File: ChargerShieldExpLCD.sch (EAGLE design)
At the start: 107 parts, among them IC1 TL431, IC2 LM324N, Q1 BUZ11, Q2 BD648, Q3 BUZ171, Q4 IRFZ48Z, T1 BC548, X1 +Vin, X2 VCC, X3 Battery

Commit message: rearranged power transistors
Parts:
- D1: device diode:SCHOTTKY-DIODEDO35-7 -> diode:SCHOTTKY-DIODEF126Z12
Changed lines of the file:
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@@
 <grid distance="0.05" unitdist="inch" unit="mm" style="lines" multiple="1" display="yes" altdistance="0.025" altunitdist="inch" altunit="mm"/>
 <layers>
-<layer number="1" name="Top" color="4" fill="1" visible="no" active="no"/>
-<layer number="2" name="Route2" color="1" fill="3" visible="no" active="no"/>
-<layer number="3" name="Route3" color="4" fill="3" visible="no" active="no"/>
-<layer number="4" name="Route4" color="1" fill="4" visible="no" active="no"/>
-<layer number="5" name="Route5" color="4" fill="4" visible="no" active="no"/>
-<layer number="6" name="Route6" color="1" fill="8" visible="no" active="no"/>
-<layer number="7" name="Route7" color="4" fill="8" visible="no" active="no"/>
-<layer number="8" name="Route8" color="1" fill="2" visible="no" active="no"/>
-<layer number="9" name="Route9" color="4" fill="2" visible="no" active="no"/>
-<layer number="10" name="Route10" color="1" fill="7" visible="no" active="no"/>
-<layer number="11" name="Route11" color="4" fill="7" visible="no" active="no"/>
-<layer number="12" name="Route12" color="1" fill="5" visible="no" active="no"/>
-<layer number="13" name="Route13" color="4" fill="5" visible="no" active="no"/>
-<layer number="14" name="Route14" color="1" fill="6" visible="no" active="no"/>
-<layer number="15" name="Route15" color="4" fill="6" visible="no" active="no"/>
-<layer number="16" name="Bottom" color="1" fill="1" visible="no" active="no"/>
-<layer number="17" name="Pads" color="2" fill="1" visible="no" active="no"/>
-<layer number="18" name="Vias" color="2" fill="1" visible="no" active="no"/>
-<layer number="19" name="Unrouted" color="6" fill="1" visible="no" active="no"/>
-<layer number="20" name="Dimension" color="15" fill="1" visible="no" active="no"/>
-<layer number="21" name="tPlace" color="7" fill="1" visible="no" active="no"/>
-<layer number="22" name="bPlace" color="7" fill="1" visible="no" active="no"/>
-<layer number="23" name="tOrigins" color="15" fill="1" visible="no" active="no"/>
-<layer number="24" name="bOrigins" color="15" fill="1" visible="no" active="no"/>
-<layer number="25" name="tNames" color="7" fill="1" visible="no" active="no"/>
-<layer number="26" name="bNames" color="7" fill="1" visible="no" active="no"/>
-<layer number="27" name="tValues" color="7" fill="1" visible="no" active="no"/>
-<layer number="28" name="bValues" color="7" fill="1" visible="no" active="no"/>
+<layer number="1" name="Top" color="4" fill="1" visible="yes" active="no"/>
+<layer number="2" name="Route2" color="1" fill="3" visible="yes" active="no"/>
+<layer number="3" name="Route3" color="4" fill="3" visible="yes" active="no"/>
+<layer number="4" name="Route4" color="1" fill="4" visible="yes" active="no"/>
+<layer number="5" name="Route5" color="4" fill="4" visible="yes" active="no"/>
+<layer number="6" name="Route6" color="1" fill="8" visible="yes" active="no"/>
+<layer number="7" name="Route7" color="4" fill="8" visible="yes" active="no"/>
+<layer number="8" name="Route8" color="1" fill="2" visible="yes" active="no"/>
+<layer number="9" name="Route9" color="4" fill="2" visible="yes" active="no"/>
+<layer number="10" name="Route10" color="1" fill="7" visible="yes" active="no"/>
+<layer number="11" name="Route11" color="4" fill="7" visible="yes" active="no"/>
+<layer number="12" name="Route12" color="1" fill="5" visible="yes" active="no"/>
+<layer number="13" name="Route13" color="4" fill="5" visible="yes" active="no"/>
+<layer number="14" name="Route14" color="1" fill="6" visible="yes" active="no"/>
+<layer number="15" name="Route15" color="4" fill="6" visible="yes" active="no"/>
+<layer number="16" name="Bottom" color="1" fill="1" visible="yes" active="no"/>
+<layer number="17" name="Pads" color="2" fill="1" visible="yes" active="no"/>
+<layer number="18" name="Vias" color="2" fill="1" visible="yes" active="no"/>
+<layer number="19" name="Unrouted" color="6" fill="1" visible="yes" active="no"/>
+<layer number="20" name="Dimension" color="15" fill="1" visible="yes" active="no"/>
+<layer number="21" name="tPlace" color="7" fill="1" visible="yes" active="no"/>
+<layer number="22" name="bPlace" color="7" fill="1" visible="yes" active="no"/>
+<layer number="23" name="tOrigins" color="15" fill="1" visible="yes" active="no"/>
+<layer number="24" name="bOrigins" color="15" fill="1" visible="yes" active="no"/>
+<layer number="25" name="tNames" color="7" fill="1" visible="yes" active="no"/>
+<layer number="26" name="bNames" color="7" fill="1" visible="yes" active="no"/>
+<layer number="27" name="tValues" color="7" fill="1" visible="yes" active="no"/>
+<layer number="28" name="bValues" color="7" fill="1" visible="yes" active="no"/>
 <layer number="29" name="tStop" color="7" fill="3" visible="no" active="no"/>
 <layer number="30" name="bStop" color="7" fill="6" visible="no" active="no"/>
@@
 <layer number="35" name="tGlue" color="7" fill="4" visible="no" active="no"/>
 <layer number="36" name="bGlue" color="7" fill="5" visible="no" active="no"/>
-<layer number="37" name="tTest" color="7" fill="1" visible="no" active="no"/>
-<layer number="38" name="bTest" color="7" fill="1" visible="no" active="no"/>
+<layer number="37" name="tTest" color="7" fill="1" visible="yes" active="no"/>
+<layer number="38" name="bTest" color="7" fill="1" visible="yes" active="no"/>
 <layer number="39" name="tKeepout" color="4" fill="11" visible="no" active="no"/>
 <layer number="40" name="bKeepout" color="1" fill="11" visible="no" active="no"/>
@@
 <layer number="44" name="Drills" color="7" fill="1" visible="no" active="no"/>
 <layer number="45" name="Holes" color="7" fill="1" visible="no" active="no"/>
-<layer number="46" name="Milling" color="3" fill="1" visible="no" active="no"/>
-<layer number="47" name="Measures" color="7" fill="1" visible="no" active="no"/>
-<layer number="48" name="Document" color="7" fill="1" visible="no" active="no"/>
-<layer number="49" name="Reference" color="7" fill="1" visible="no" active="no"/>
-<layer number="50" name="dxf" color="7" fill="1" visible="no" active="no"/>
-<layer number="51" name="tDocu" color="7" fill="1" visible="no" active="no"/>
-<layer number="52" name="bDocu" color="7" fill="1" visible="no" active="no"/>
-<layer number="53" name="tGND_GNDA" color="7" fill="9" visible="no" active="no"/>
-<layer number="54" name="bGND_GNDA" color="1" fill="9" visible="no" active="no"/>
-<layer number="56" name="wert" color="7" fill="1" visible="no" active="no"/>
-<layer number="57" name="tCAD" color="7" fill="1" visible="no" active="no"/>
+<layer number="46" name="Milling" color="3" fill="1" visible="yes" active="no"/>
+<layer number="47" name="Measures" color="7" fill="1" visible="yes" active="no"/>
+<layer number="48" name="Document" color="7" fill="1" visible="yes" active="no"/>
+<layer number="49" name="Reference" color="7" fill="1" visible="yes" active="no"/>
+<layer number="50" name="dxf" color="7" fill="1" visible="yes" active="no"/>
+<layer number="51" name="tDocu" color="7" fill="1" visible="yes" active="no"/>
+<layer number="52" name="bDocu" color="7" fill="1" visible="yes" active="no"/>
+<layer number="53" name="tGND_GNDA" color="7" fill="9" visible="yes" active="no"/>
+<layer number="54" name="bGND_GNDA" color="1" fill="9" visible="yes" active="no"/>
+<layer number="56" name="wert" color="7" fill="1" visible="yes" active="no"/>
+<layer number="57" name="tCAD" color="7" fill="1" visible="yes" active="no"/>
 <layer number="91" name="Nets" color="2" fill="1" visible="yes" active="yes"/>
 <layer number="92" name="Busses" color="1" fill="1" visible="yes" active="yes"/>
@@
 <part name="R16" library="rcl" deviceset="R-EU_" device="0207/10" value="1k"/>
 <part name="Q2" library="transistor-pnp" deviceset="BD648" device=""/>
-<part name="D1" library="diode" deviceset="SCHOTTKY-DIODE" device="DO35-7"/>
+<part name="D1" library="diode" deviceset="SCHOTTKY-DIODE" device="F126Z12"/>
 <part name="L1" library="rcl" deviceset="L-EU" device="0207/12" value="100µ"/>
 <part name="V1" library="Misc" deviceset="CELL" device=""/>

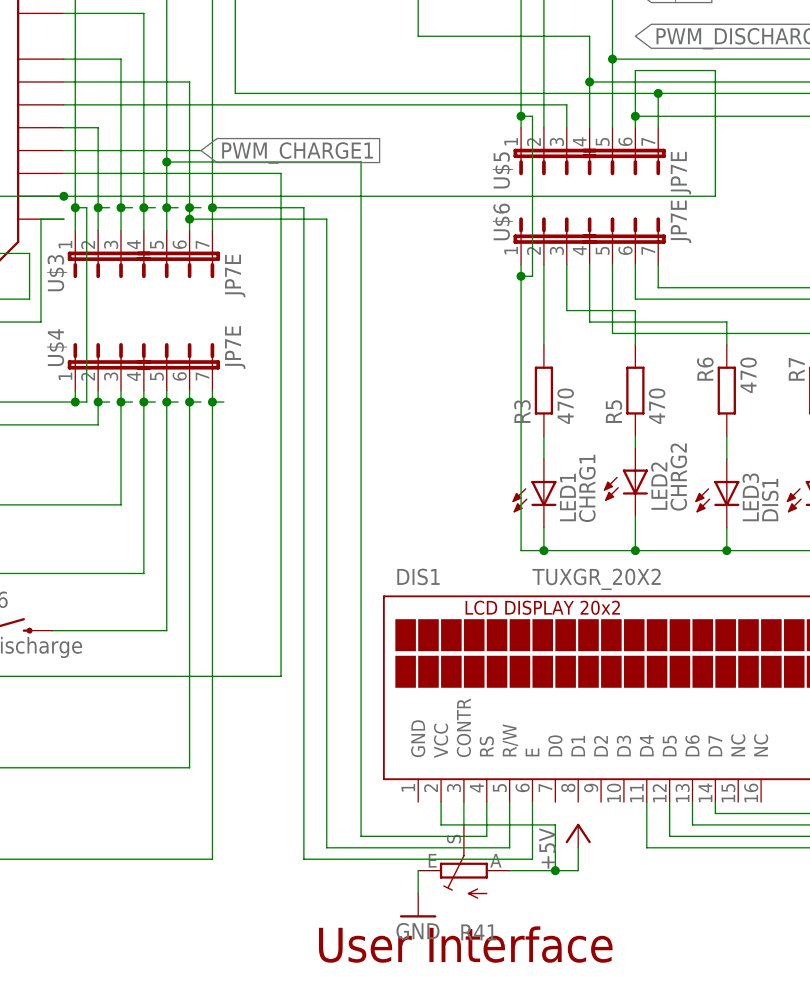
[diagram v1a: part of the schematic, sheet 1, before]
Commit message: jumper to switch LCD RS Pin
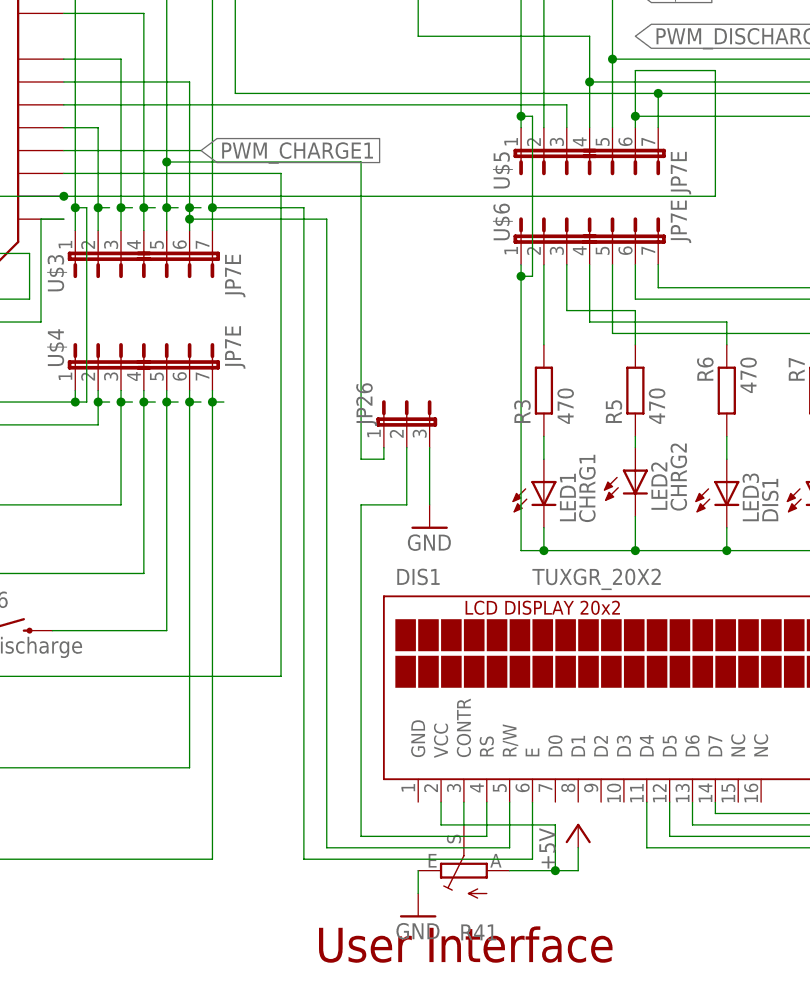
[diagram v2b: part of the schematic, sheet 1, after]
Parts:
- added JP26: (no value), bigger:JP2E
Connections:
- new net N$63: DIS1.RS, JP26.2
- net GND: now also JP26.3
- net N$67: now also JP26.1; no longer DIS1.RS
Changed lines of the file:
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@@
 <grid distance="0.05" unitdist="inch" unit="mm" style="lines" multiple="1" display="yes" altdistance="0.025" altunitdist="inch" altunit="mm"/>
 <layers>
-<layer number="1" name="Top" color="4" fill="1" visible="yes" active="no"/>
-<layer number="2" name="Route2" color="1" fill="3" visible="yes" active="no"/>
-<layer number="3" name="Route3" color="4" fill="3" visible="yes" active="no"/>
-<layer number="4" name="Route4" color="1" fill="4" visible="yes" active="no"/>
-<layer number="5" name="Route5" color="4" fill="4" visible="yes" active="no"/>
-<layer number="6" name="Route6" color="1" fill="8" visible="yes" active="no"/>
-<layer number="7" name="Route7" color="4" fill="8" visible="yes" active="no"/>
-<layer number="8" name="Route8" color="1" fill="2" visible="yes" active="no"/>
-<layer number="9" name="Route9" color="4" fill="2" visible="yes" active="no"/>
-<layer number="10" name="Route10" color="1" fill="7" visible="yes" active="no"/>
-<layer number="11" name="Route11" color="4" fill="7" visible="yes" active="no"/>
-<layer number="12" name="Route12" color="1" fill="5" visible="yes" active="no"/>
-<layer number="13" name="Route13" color="4" fill="5" visible="yes" active="no"/>
-<layer number="14" name="Route14" color="1" fill="6" visible="yes" active="no"/>
-<layer number="15" name="Route15" color="4" fill="6" visible="yes" active="no"/>
-<layer number="16" name="Bottom" color="1" fill="1" visible="yes" active="no"/>
-<layer number="17" name="Pads" color="2" fill="1" visible="yes" active="no"/>
-<layer number="18" name="Vias" color="2" fill="1" visible="yes" active="no"/>
-<layer number="19" name="Unrouted" color="6" fill="1" visible="yes" active="no"/>
-<layer number="20" name="Dimension" color="15" fill="1" visible="yes" active="no"/>
-<layer number="21" name="tPlace" color="7" fill="1" visible="yes" active="no"/>
-<layer number="22" name="bPlace" color="7" fill="1" visible="yes" active="no"/>
-<layer number="23" name="tOrigins" color="15" fill="1" visible="yes" active="no"/>
-<layer number="24" name="bOrigins" color="15" fill="1" visible="yes" active="no"/>
-<layer number="25" name="tNames" color="7" fill="1" visible="yes" active="no"/>
-<layer number="26" name="bNames" color="7" fill="1" visible="yes" active="no"/>
-<layer number="27" name="tValues" color="7" fill="1" visible="yes" active="no"/>
-<layer number="28" name="bValues" color="7" fill="1" visible="yes" active="no"/>
+<layer number="1" name="Top" color="4" fill="1" visible="no" active="no"/>
+<layer number="2" name="Route2" color="1" fill="3" visible="no" active="no"/>
+<layer number="3" name="Route3" color="4" fill="3" visible="no" active="no"/>
+<layer number="4" name="Route4" color="1" fill="4" visible="no" active="no"/>
+<layer number="5" name="Route5" color="4" fill="4" visible="no" active="no"/>
+<layer number="6" name="Route6" color="1" fill="8" visible="no" active="no"/>
+<layer number="7" name="Route7" color="4" fill="8" visible="no" active="no"/>
+<layer number="8" name="Route8" color="1" fill="2" visible="no" active="no"/>
+<layer number="9" name="Route9" color="4" fill="2" visible="no" active="no"/>
+<layer number="10" name="Route10" color="1" fill="7" visible="no" active="no"/>
+<layer number="11" name="Route11" color="4" fill="7" visible="no" active="no"/>
+<layer number="12" name="Route12" color="1" fill="5" visible="no" active="no"/>
+<layer number="13" name="Route13" color="4" fill="5" visible="no" active="no"/>
+<layer number="14" name="Route14" color="1" fill="6" visible="no" active="no"/>
+<layer number="15" name="Route15" color="4" fill="6" visible="no" active="no"/>
+<layer number="16" name="Bottom" color="1" fill="1" visible="no" active="no"/>
+<layer number="17" name="Pads" color="2" fill="1" visible="no" active="no"/>
+<layer number="18" name="Vias" color="2" fill="1" visible="no" active="no"/>
+<layer number="19" name="Unrouted" color="6" fill="1" visible="no" active="no"/>
+<layer number="20" name="Dimension" color="15" fill="1" visible="no" active="no"/>
+<layer number="21" name="tPlace" color="7" fill="1" visible="no" active="no"/>
+<layer number="22" name="bPlace" color="7" fill="1" visible="no" active="no"/>
+<layer number="23" name="tOrigins" color="15" fill="1" visible="no" active="no"/>
+<layer number="24" name="bOrigins" color="15" fill="1" visible="no" active="no"/>
+<layer number="25" name="tNames" color="7" fill="1" visible="no" active="no"/>
+<layer number="26" name="bNames" color="7" fill="1" visible="no" active="no"/>
+<layer number="27" name="tValues" color="7" fill="1" visible="no" active="no"/>
+<layer number="28" name="bValues" color="7" fill="1" visible="no" active="no"/>
 <layer number="29" name="tStop" color="7" fill="3" visible="no" active="no"/>
 <layer number="30" name="bStop" color="7" fill="6" visible="no" active="no"/>
@@
 <layer number="35" name="tGlue" color="7" fill="4" visible="no" active="no"/>
 <layer number="36" name="bGlue" color="7" fill="5" visible="no" active="no"/>
-<layer number="37" name="tTest" color="7" fill="1" visible="yes" active="no"/>
-<layer number="38" name="bTest" color="7" fill="1" visible="yes" active="no"/>
+<layer number="37" name="tTest" color="7" fill="1" visible="no" active="no"/>
+<layer number="38" name="bTest" color="7" fill="1" visible="no" active="no"/>
 <layer number="39" name="tKeepout" color="4" fill="11" visible="no" active="no"/>
 <layer number="40" name="bKeepout" color="1" fill="11" visible="no" active="no"/>
@@
 <layer number="44" name="Drills" color="7" fill="1" visible="no" active="no"/>
 <layer number="45" name="Holes" color="7" fill="1" visible="no" active="no"/>
-<layer number="46" name="Milling" color="3" fill="1" visible="yes" active="no"/>
-<layer number="47" name="Measures" color="7" fill="1" visible="yes" active="no"/>
-<layer number="48" name="Document" color="7" fill="1" visible="yes" active="no"/>
-<layer number="49" name="Reference" color="7" fill="1" visible="yes" active="no"/>
-<layer number="50" name="dxf" color="7" fill="1" visible="yes" active="no"/>
-<layer number="51" name="tDocu" color="7" fill="1" visible="yes" active="no"/>
-<layer number="52" name="bDocu" color="7" fill="1" visible="yes" active="no"/>
-<layer number="53" name="tGND_GNDA" color="7" fill="9" visible="yes" active="no"/>
-<layer number="54" name="bGND_GNDA" color="1" fill="9" visible="yes" active="no"/>
-<layer number="56" name="wert" color="7" fill="1" visible="yes" active="no"/>
-<layer number="57" name="tCAD" color="7" fill="1" visible="yes" active="no"/>
+<layer number="46" name="Milling" color="3" fill="1" visible="no" active="no"/>
+<layer number="47" name="Measures" color="7" fill="1" visible="no" active="no"/>
+<layer number="48" name="Document" color="7" fill="1" visible="no" active="no"/>
+<layer number="49" name="Reference" color="7" fill="1" visible="no" active="no"/>
+<layer number="50" name="dxf" color="7" fill="1" visible="no" active="no"/>
+<layer number="51" name="tDocu" color="7" fill="1" visible="no" active="no"/>
+<layer number="52" name="bDocu" color="7" fill="1" visible="no" active="no"/>
+<layer number="53" name="tGND_GNDA" color="7" fill="9" visible="no" active="no"/>
+<layer number="54" name="bGND_GNDA" color="1" fill="9" visible="no" active="no"/>
+<layer number="56" name="wert" color="7" fill="1" visible="no" active="no"/>
+<layer number="57" name="tCAD" color="7" fill="1" visible="no" active="no"/>
 <layer number="91" name="Nets" color="2" fill="1" visible="yes" active="yes"/>
 <layer number="92" name="Busses" color="1" fill="1" visible="yes" active="yes"/>
@@
 <part name="GND19" library="supply1" deviceset="GND" device=""/>
 <part name="P+11" library="supply1" deviceset="+5V" device=""/>
+<part name="JP26" library="bigger" deviceset="JP2E" device=""/>
+<part name="GND20" library="supply1" deviceset="GND" device=""/>
 </parts>
 <sheets>
@@
 <instance part="GND19" gate="1" x="191.77" y="31.75"/>
 <instance part="P+11" gate="1" x="209.55" y="41.91"/>
+<instance part="JP26" gate="1" x="190.5" y="86.36"/>
+<instance part="GND20" gate="1" x="193.04" y="74.93"/>
 </instances>
 <busses>
@@
 <wire x1="191.77" y1="36.83" x2="191.77" y2="34.29" width="0.1524" layer="91"/>
 </segment>
+<segment>
+<pinref part="JP26" gate="1" pin="3"/>
+<pinref part="GND20" gate="1" pin="GND"/>
+<wire x1="193.04" y1="83.82" x2="193.04" y2="77.47" width="0.1524" layer="91"/>
+</segment>
 </net>
 <net name="N$1" class="0">
@@
 <net name="N$67" class="0">
 <segment>
-<pinref part="DIS1" gate="G$1" pin="RS"/>
-<wire x1="199.39" y1="44.45" x2="199.39" y2="40.64" width="0.1524" layer="91"/>
-<wire x1="199.39" y1="40.64" x2="185.42" y2="40.64" width="0.1524" layer="91"/>
 <pinref part="U$2" gate="G$1" pin="D12"/>
 <wire x1="152.4" y1="142.24" x2="163.83" y2="142.24" width="0.1524" layer="91"/>
@@
 <wire x1="163.83" y1="110.49" x2="165.1" y2="110.49" width="0.1524" layer="91"/>
 <junction x="163.83" y="110.49"/>
-<wire x1="185.42" y1="40.64" x2="185.42" y2="115.57" width="0.1524" layer="91"/>
+<wire x1="185.42" y1="82.55" x2="185.42" y2="115.57" width="0.1524" layer="91"/>
 <wire x1="185.42" y1="115.57" x2="163.83" y2="115.57" width="0.1524" layer="91"/>
 <junction x="163.83" y="115.57"/>
+<wire x1="185.42" y1="82.55" x2="187.96" y2="82.55" width="0.1524" layer="91"/>
+<pinref part="JP26" gate="1" pin="1"/>
+<wire x1="187.96" y1="82.55" x2="187.96" y2="83.82" width="0.1524" layer="91"/>
 </segment>
 </net>
@@
 </segment>
 </net>
+<net name="N$63" class="0">
+<segment>
+<pinref part="DIS1" gate="G$1" pin="RS"/>
+<wire x1="199.39" y1="44.45" x2="199.39" y2="40.64" width="0.1524" layer="91"/>
+<wire x1="199.39" y1="40.64" x2="185.42" y2="40.64" width="0.1524" layer="91"/>
+<wire x1="185.42" y1="40.64" x2="185.42" y2="77.47" width="0.1524" layer="91"/>
+<pinref part="JP26" gate="1" pin="2"/>
+<wire x1="190.5" y1="83.82" x2="190.5" y2="77.47" width="0.1524" layer="91"/>
+<wire x1="190.5" y1="77.47" x2="185.42" y2="77.47" width="0.1524" layer="91"/>
+</segment>
+</net>
